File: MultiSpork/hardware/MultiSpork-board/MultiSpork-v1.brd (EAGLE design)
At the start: 160 x 100 mm, 108 parts, among them U1 USD-SOCKETNEW, U2 SAM3SA-MU, U3 MAX11300GTL, U4 MIC2954, U5 MIC5201-3.3BS, U7 MCP73831

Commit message: Updated board with: 	-- Voltage regulators 	-- CC3100 WiFi
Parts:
- added C37, C40, C41, C42, C45, C46, C48, C51, C52, C54, C57, C58, C60, C61, C62: (no value), resistor:C1210
- added C38, C39, C43, C44, C47, C49, C50, C53, C55, C56, C59: (no value), resistor:C0603
- added C63, C67, C69, C70, C71, C73, C74, C75, C76, C77, C80: 100n, resistor:C0603
- added C64, C65, C66: 4u7, resistor:C0603
- added C68, C72: 10u, resistor:C0603
- added C78, C79: 22u, resistor:C1206
- added D15, D16, D17, D18, D19: (no value), diode:SMB
- added JP2: (no value), pinhead:1X06
- added JP3: (no value), pinhead:1X04
- added L10, L12: 2u2, SparkFun-Passives:INDUCTOR-1206
- added L11: 1u, SparkFun-Passives:INDUCTOR-1206
- added L3, L4, L5, L6, L7, L8, L9: NR6028, logos-inductors:NR60XX
- added R1, R14, R15, R16, R17, R18, R19, R20, R21, R22, R23, R24: (no value), resistor:R0603
- added R25, R32: 10K, resistor:R0603
- added R26, R27, R28, R31, R33, R34, R35: 100K, resistor:R0603
- added R29, R30: 4K7, resistor:R0603
- added U6, U8: LT3580EMS8E, MultiSpork-parts:MSOP8
- added U9: CC3100, CC3100:QFN64
- F2: value 500 mA -> 1500 mA
- U4: value MIC2954 -> LT3580EMS8E; device logos-power:SOT223 -> MultiSpork-parts:MSOP8
- U5: value MIC5201-3.3BS -> LT3580EMS8E; device logos-power:SOT223 -> MultiSpork-parts:MSOP8
- moved U3 179.4 mm to (64.8, 30.5)
- moved U5 114.1 mm to (-176.5, -364.5)
- moved U4 58.5 mm to (-168.9, -306.1)
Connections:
- removed net RXD: R6.4
- removed net TXD: R6.6
- new net CC_CS: U2.36, U9.8
- new net CC_INT: R25.2, U2.32, U9.15
- new net CC_NHIB: R28.1, U2.35, U9.2
- new net CC_RST: C80.1, JP2.5, R27.1, U2.24, U9.32
- new net DCDC_ANA2_SW_N: U9.46
- new net DCDC_ANA2_SW_P: U9.45
- new net N$100: JP3.3, U9.59
- new net N$101: JP3.4, U9.58
- new net N$102: R35.2, U9.3
- new net N$106: JP2.1, U9.50
- new net N$107: JP2.2, U9.55
- new net N$108: JP2.3, U9.57
- new net N$109: JP2.4, U9.61
- new net N$18: C38.1, U4.7
- new net N$20: R1.2, U4.6
- new net N$21: R14.1, U4.1
- new net N$22: R15.1, U4.2
- new net N$23: C39.1, R15.2
- new net N$24: C43.1, U5.7
- new net N$25: D16.A, L3.2, U4.4
- new net N$26: R16.2, U5.6
- new net N$28: R17.1, U5.1
- new net N$60: C47.1, R18.1, U5.2
- new net N$61: C44.1, R18.2
- new net N$63: C45.1, L4.2, U5.4
- new net N$64: C45.2, D17.A, L5.1
- new net N$65: C55.1, U8.7
- new net N$66: R22.2, U8.6
- new net N$67: R23.1, U8.1
- new net N$68: C49.1, U6.7
- new net N$69: R19.2, U6.6
- new net N$70: R20.1, U6.1
- new net N$71: C53.1, R21.1, U6.2
- new net N$72: C50.1, R21.2
- new net N$73: C51.1, L6.2, U6.4
- new net N$74: C51.2, D18.A, L7.1
- new net N$75: C59.1, R24.1, U8.2
- new net N$76: C56.1, R24.2
- new net N$77: C58.1, L8.2, U8.4
- new net N$78: C58.2, D19.A, L9.1
- new net N$79: C63.1, U9.54
- new net N$80: C64.1, U9.44
- new net N$81: C66.1, U9.37
- new net N$82: C67.1, C68.1, C69.1, C70.1, C71.1, L10.P$1, U9.10, U9.25, U9.36, U9.48
- new net N$83: C65.1, U9.39
- new net N$84: L10.P$2, U9.38
- new net N$85: C77.1, C78.1, C79.1, U9.33, U9.42
- new net N$87: L11.P$1, U9.40
- new net N$88: L11.P$2, U9.41
- new net N$89: L12.P$2, U9.43
- new net N$90: C72.1, C73.1, C74.1, L12.P$1, U9.56, U9.9
- new net N$91: R31.2, U9.4
- new net N$92: C75.1, U9.49
- new net N$93: C76.1, U9.24
- new net N$94: R32.2, U9.21
- new net N$95: R33.2, U9.34
- new net N$96: R34.2, U9.35
- new net N$98: JP3.1, U9.62
- new net N$99: JP3.2, U9.60
- new net RXD0: R6.4, U2.27
- new net TXD0: R6.6, U2.26
- net +10V: now also C40.1, C41.1, D16.C, R14.2
- net +3V3: now also C52.1, C62.1, D18.C, R20.2, R27.2, R28.2, R29.2, R30.2, U9.47; no longer U5.3
- net +5V: now also C46.1, C61.1, D17.C, R17.2; no longer U4.3
- net +UB: now also D15.A
- net -10V: now also C57.2, C60.2, L9.2, R23.2
- net ACC_CS: now also U2.21
- net GND: now also C37.2, C38.2, C39.2, C40.2, C41.2, C42.2, C43.2, C44.2, C46.2, C47.2, C48.2, C49.2, C50.2, C52.2, C53.2, C54.2, C55.2, C56.2, C57.1, C59.2, C60.1, C61.2, C62.2, C63.2, C64.2, C65.2, C66.2, C67.2, C68.2, C69.2, C70.2, C71.2, C72.2, C73.2, C74.2, C75.2, C76.2, C77.2, C78.2, C79.2, C80.2, D19.C, JP2.6, L5.2, L7.2, R1.1, R16.1, R19.1, R22.1, R25.1, R26.1, R31.1, R32.1, R33.1, R34.1, R35.1, U4.8, U4.EP, U5.8, U5.EP, U6.8, U6.EP, U8.8, U8.EP, U9.PAD
- net MAX_CS: now also U2.20
- net MAX_CVNT: now also U2.23
- net MAX_INT: now also U2.15
- net MISO: now also R26.2, U2.19, U9.7
- net MOSI: now also U2.17, U9.6
- net SCL: now also R30.1, U2.28
- net SCLK: now also U2.16, U9.5
- net SDA: now also R29.1, U2.31
- net SD_CS: now also U2.22
- net V+: now also C37.1, C42.1, C48.1, C54.1, D15.C, L3.1, L4.1, L6.1, L8.1, U4.3, U4.5, U5.3, U5.5, U6.3, U6.5, U8.3, U8.5

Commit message: -- Added flash chip to CC3100.lbr -- Added 2.4 GHz filter to CC3100.lbr -- Added RF components on schematic -- Added CC3100 crystals on schematic -- Added MAX11300 external temperature sensors -- Fixed some issues with the protection circuitry hookup
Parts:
- added C81, C82, C83, C84: (no value), resistor:C0603
- added C85: 100n, resistor:C0603
- added C86, C87: 100u, resistor:CT6032
- added FL1: DEA202450BT, CC3100:DEA202450BT
- added Q2: 40 MHz, logos-crystals:ECX-31B
- added Q3: 32.768 kHz, logos-crystals:CSM-3X
- added Q4, Q5: MMBT3904, SparkFun-DiscreteSemi:SOT23
- added R36: (no value), resistor:R0603
- added R37, R38, R39: 100K, resistor:R0603
- added RESET: SKHMPSE010, switch:SKHMPXE010
- added U$1: ATMEGA128RFA1_MOLEX-ANT, CC3100:ATMEGA128RFA1_MOLEX-ANT
- added U10: M25PX80, CC3100:SOIC8
- moved F10 295.6 mm to (116.8, 34.3)
- moved F11 295.6 mm to (116.8, 30.5)
- moved F12 295.6 mm to (116.8, 26.7)
- moved F3 295.6 mm to (116.8, 61.0)
- moved F4 295.6 mm to (116.8, 57.1)
- moved F5 295.6 mm to (116.8, 53.3)
- moved F6 295.6 mm to (116.8, 49.5)
- moved F7 295.6 mm to (116.8, 45.7)
- moved F8 295.6 mm to (116.8, 41.9)
- moved F9 295.6 mm to (116.8, 38.1)
- moved F22 292.9 mm to (86.4, 26.7)
- moved F20 289.6 mm to (86.4, 29.2)
- moved F21 289.6 mm to (86.4, 25.4)
- moved F18 286.4 mm to (86.4, 31.8)
- moved F19 286.4 mm to (86.4, 27.9)
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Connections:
- new net N$103: C81.1, Q2.1, U9.22
- new net N$104: C82.1, Q2.2, U9.23
- new net N$105: C83.1, Q3.1, U9.52
- new net N$110: C84.1, Q3.2, U9.51
- new net N$111: U10.2, U9.13
- new net N$112: R39.1, U10.1, U9.14
- new net N$113: FL1.1, U9.31
- new net N$114: FL1.3, U$1.A
- new net N$115: Q5.1, Q5.3, U3.19
- new net N$116: Q5.2, U3.20
- new net N$117: Q4.2, U3.13
- new net N$118: Q4.1, Q4.3, U3.12
- new net N$86: R38.2, U10.6, U9.11
- new net N$97: R37.2, U10.5, U9.12
- net +3V3: now also C29.1, C30.1, C85.1, C86.+, C87.+, R36.2, R39.2, U10.3, U10.7, U10.8, U3.2
- net +5V: no longer C29.1, C30.1, U3.2
- net GND: now also C81.2, C82.2, C83.2, C84.2, C85.2, C86.-, C87.-, FL1.2, FL1.4, R37.1, R38.1, RESET.1, RESET.2, RESET.5, U10.4
- net MASTER_RESET: now also R36.1, RESET.3, RESET.4
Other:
- board size 160 x 100 mm -> 100 x 75 mm

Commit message: Finished schematic & placement for the prototype
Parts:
- removed U$1: ATMEGA128RFA1_MOLEX-ANT, CC3100:ATMEGA128RFA1_MOLEX-ANT
- added J1: U.FL, SparkFun-Connectors:U.FL
- added R40: (no value), resistor:R1206
- ANALOG: value (none) -> 76385-316LF; device pinhead-1:2X16SMD/90 -> logos-headers:32P-SIDE-SMD
- C10, C11, C21, C27, C29, C30, C31, C32, C33, C34: device resistor:C1206 -> resistor:C0603
- D16, D18, D19: device diode:SMB -> adafruit:SMADIODE
- D17: device diode:SMB -> adafruit:SOD-123
- L3, L8: value NR6028 -> L-US2323; device logos-inductors:NR60XX -> logos-inductors:L2323
- L4, L5, L6, L7, L9: value NR6028 -> L-US1008; device logos-inductors:NR60XX -> logos-inductors:L1008
- Q2: value 40 MHz -> 32.768 kHz
- Q3: value 32.768 kHz -> 40 MHz
- moved Q5 829.6 mm to (79.5, 27.9)
- moved Q4 827.0 mm to (75.9, 27.9)
- moved C87 817.1 mm to (42.4, 32.0), turned to 180 degrees
- moved C86 814.7 mm to (42.4, 35.8), turned to 180 degrees
- moved RESET 812.7 mm to (68.6, 66.3), turned to 270 degrees
- moved R36 808.3 mm to (63.0, 68.6), turned to 180 degrees
- moved FL1 786.9 mm to (49.0, 10.4), turned to 180 degrees
- moved C85 772.4 mm to (17.0, 16.5), turned to 90 degrees
- moved R39 771.9 mm to (23.1, 7.87), turned to 180 degrees
- moved R38 768.0 mm to (18.8, 16.5), turned to 270 degrees
- moved R37 762.4 mm to (20.6, 16.5), turned to 270 degrees
- moved C84 761.2 mm to (49.8, 27.2), turned to 90 degrees
- moved C83 756.8 mm to (47.2, 27.2), turned to 90 degrees
- moved U10 750.6 mm to (23.4, 11.7), turned to 90 degrees
- moved JP3 736.3 mm to (39.9, 40.9)
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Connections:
- removed net N$56 (its old number): F7.2, F8.2, F9.2
- removed net N$59: F10.2, F11.2, F12.2, F13.2
- removed net N$62: F14.2, F15.2, F16.2
- removed net PORT0: F3.2
- removed net PORT1: F4.2
- removed net PORT2: F5.2
- removed net PORT3: F6.2
- net ACC_CS: now also R6.4; no longer R7.7
- net AGND: now also R40.1
- net GND: now also J1.P$1, J1.P$2, R40.2
- net MISO: now also R2.2, R6.8; no longer R2.8, R7.5
- net MOSI: now also R2.6; no longer R2.4
- net N$10: now also R7.6; no longer R7.4
- net N$103: now also Q3.1; no longer Q2.1
- net N$104: now also Q3.2; no longer Q2.2
- net N$105: now also Q2.1; no longer Q3.1
- net N$11: now also R6.7; no longer R7.6
- net N$110: now also Q2.2; no longer Q3.2
- net N$114: now also J1.P$3; no longer U$1.A
- net N$12: now also R6.3; no longer R7.8
- net N$13: now also R6.1; no longer R6.2
- net N$14: now also R7.8; no longer R6.5
- net N$15: now also R7.4; no longer R6.3
- net N$16: now also R6.5; no longer R6.7
- net N$2: now also R2.7; no longer R2.1
- net N$25: now also L3.4; no longer L3.2
- net N$4: now also R2.5; no longer R2.3
- net N$5: now also R2.3; no longer R2.5
- net N$6: now also R2.1; no longer R2.7
- net N$77: now also L8.4; no longer L8.2
- net PORT00: now also F3.2
- net PORT01: now also F4.2
- net PORT02: now also F5.2
- net PORT03: now also F6.2
- net PORT04: now also F7.2
- net PORT05: now also F8.2
- net PORT06: now also F9.2
- net PORT07: now also F10.2
- net PORT08: now also F11.2
- net PORT09: now also F12.2
- net PORT10: now also F13.2
- net PORT11: now also F14.2
- net PORT12: now also F15.2
- net PORT13: now also F16.2
- net RXD0: now also R7.3; no longer R6.4
- net SCL: now also R6.6; no longer R6.8
- net SCLK: now also R2.4, R7.5; no longer R2.6, R7.3
- net SDA: now also R6.2; no longer R6.1
- net SD_CS: now also R2.8; no longer R2.2
- net TXD0: now also R7.7; no longer R6.6
- net V+: now also L3.3, L8.3; no longer L3.1, L8.1
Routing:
- added copper zone on layer 1, net AGND
- added copper zone on layer 16, net AGND
- added copper zone on layer 1, net GND
- added copper zone on layer 16, net GND
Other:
- board size 100 x 75 mm -> 101.6 x 76.2 mm

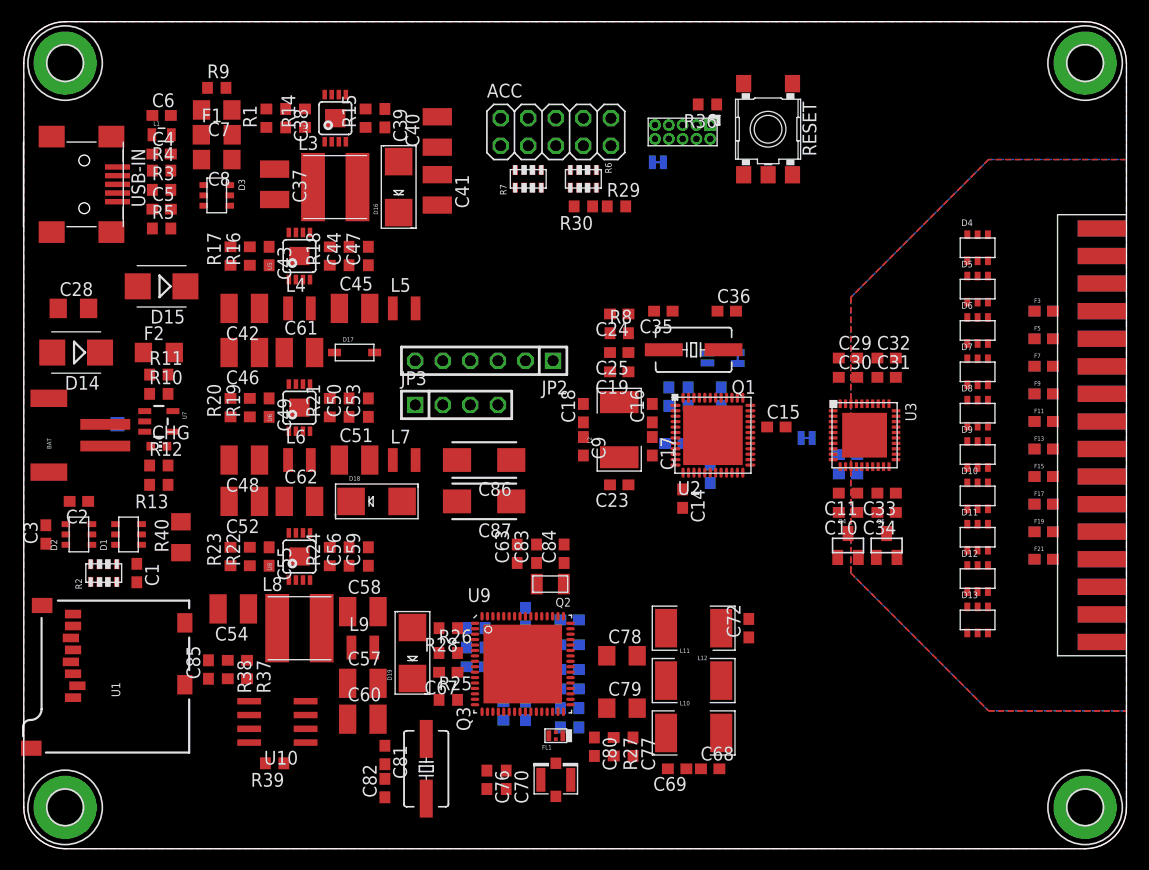
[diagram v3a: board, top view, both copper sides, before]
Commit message: Shrank the board from 3x4 to 3x3.4
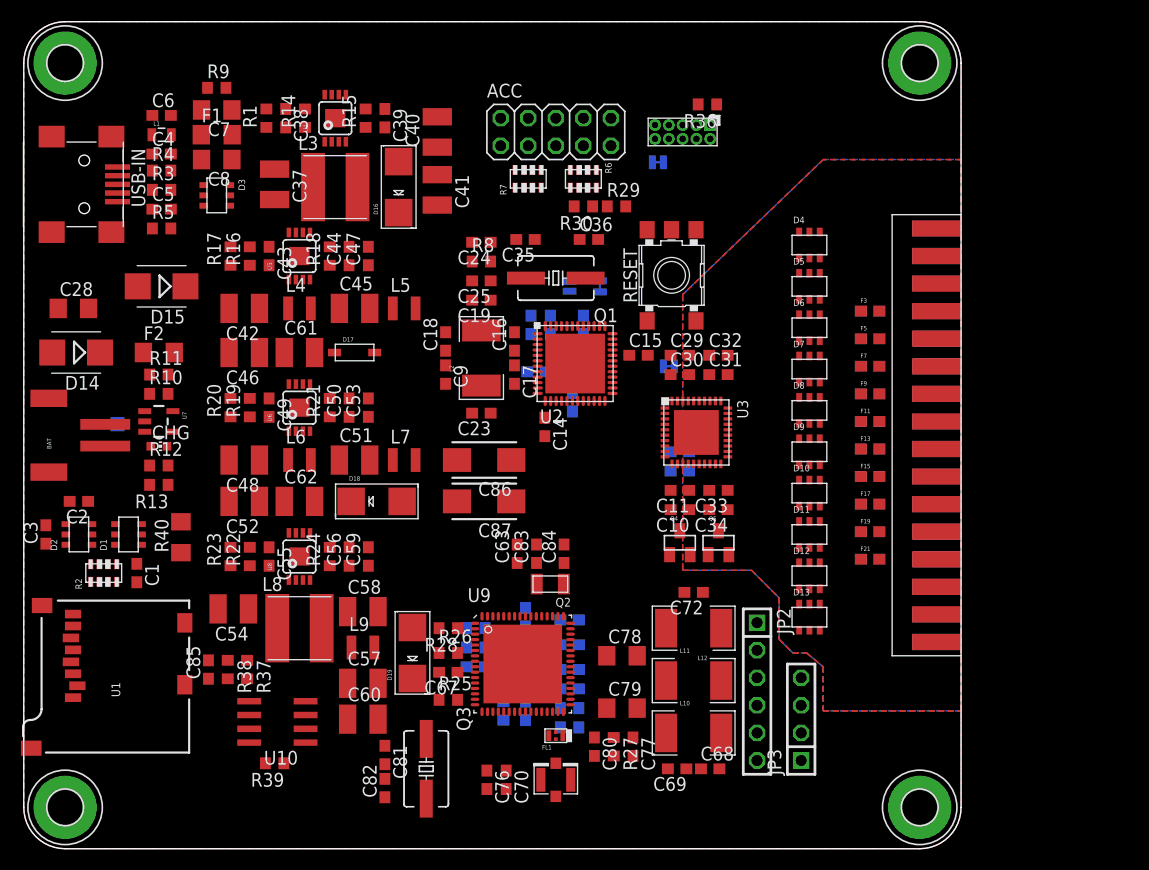
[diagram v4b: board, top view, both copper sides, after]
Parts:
- moved JP3 43.0 mm to (71.6, 11.9), turned to 90 degrees
- moved JP2 39.5 mm to (67.6, 14.5), turned to 270 degrees
- moved RESET 16.1 mm to (59.7, 52.8), turned to 90 degrees
- moved F10 16.0 mm to (78.0, 41.9)
- moved F11 16.0 mm to (78.0, 39.4)
- moved F12 16.0 mm to (78.0, 39.4)
- moved F13 16.0 mm to (78.0, 36.8)
- moved F14 16.0 mm to (78.0, 36.8)
- moved F15 16.0 mm to (78.0, 34.3)
- moved F16 16.0 mm to (78.0, 34.3)
- moved F17 16.0 mm to (78.0, 31.8)
- moved F18 16.0 mm to (78.0, 31.8)
- moved F19 16.0 mm to (78.0, 29.2)
- moved F20 16.0 mm to (78.0, 29.2)
- moved F21 16.0 mm to (78.0, 26.7)
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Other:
- board size 101.6 x 76.2 mm -> 86.4 x 76.2 mm

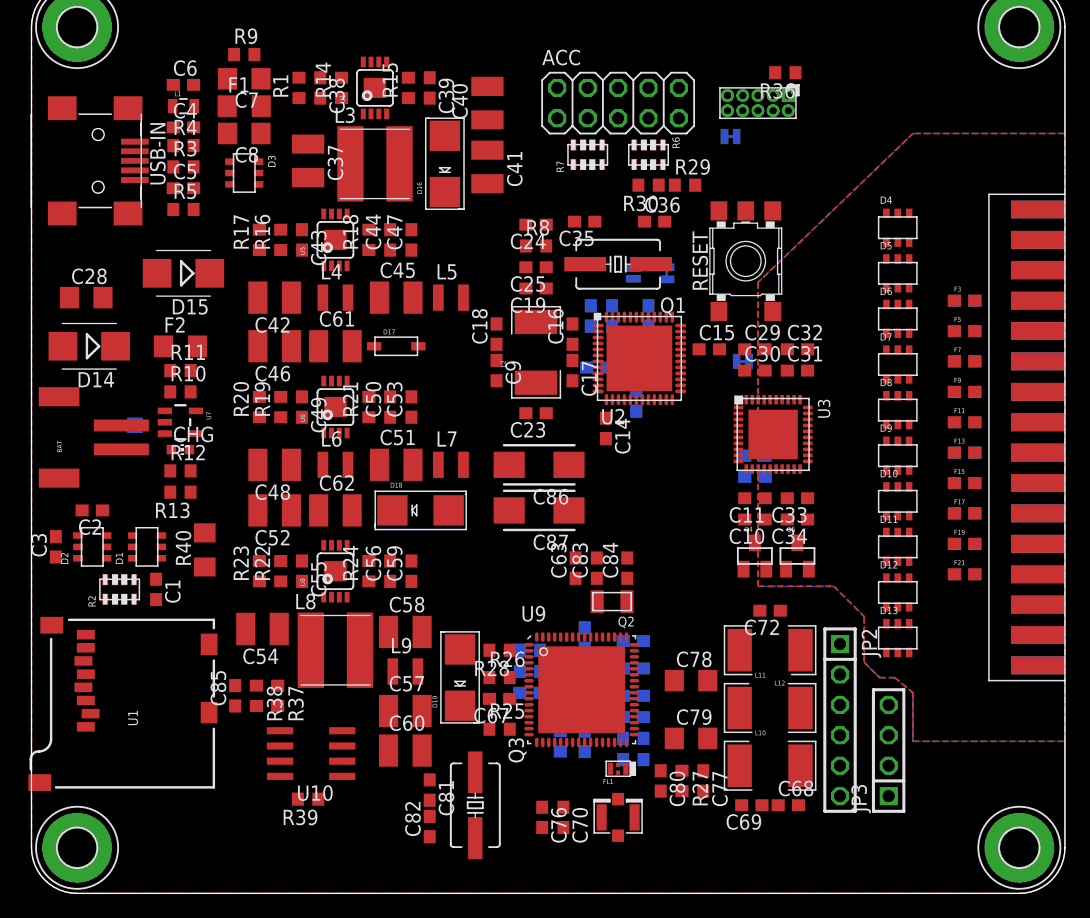
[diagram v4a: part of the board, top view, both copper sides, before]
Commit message: -- Updated MAX11300 footprint with rounded pads to account for minimum clearances at the corners -- Added a switch to turn the regulators on and off -- Routed USB -- Routed SPI busses -- Routed analog inputs to protection components
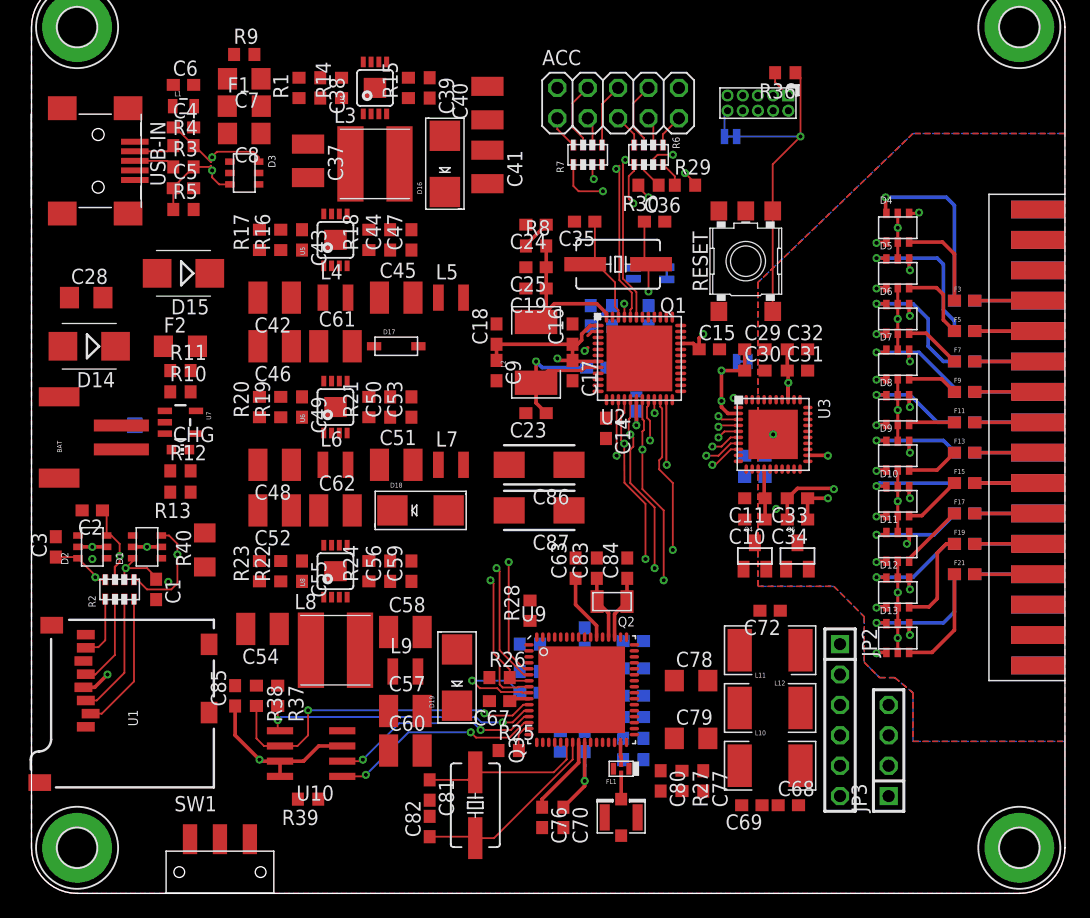
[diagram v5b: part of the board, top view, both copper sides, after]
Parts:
- added SW1: JS102011SAQN, logos-switch:JS102011SAQN
- moved R28 4.17 mm to (41.7, 23.6), turned to 90 degrees
- moved R25 1.93 mm to (39.9, 11.9)
- moved R35 0.51 mm to (41.7, 20.8)
- moved FL1 0.25 mm to (49.3, 10.4)
- moved J1 0.25 mm to (49.3, 6.35)
- moved D19 0.25 mm to (35.6, 18.0)
- moved C67 0.19 mm to (39.1, 16.1)
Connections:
- new net SHTDWN: SW1.2, U4.5, U5.5, U6.5, U8.5
- net GND: now also SW1.1
- net V+: now also SW1.3; no longer U4.5, U5.5, U6.5, U8.5
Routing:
- net MISO: track 0.00 -> 113.0 mm, vias 0 -> 6
- net MOSI: track 0.00 -> 110.7 mm, vias 0 -> 6
- net SCLK: track 0.00 -> 110.4 mm, vias 0 -> 6
- net SD_CS: track 0.00 -> 64.1 mm, vias 0 -> 2
- net USB_N: track 0.00 -> 58.2 mm, vias 0 -> 2
- net +3V3: track 0.00 -> 57.1 mm, vias 0 -> 10
- net USB_P: track 0.00 -> 56.9 mm, vias 0 -> 2
- net +10V: track 0.00 -> 40.9 mm, vias 0 -> 9
- net -10V: track 0.00 -> 34.2 mm, vias 0 -> 22
- net N$86: track 0.00 -> 28.8 mm, vias 0 -> 2
- net MASTER_RESET: track 0.00 -> 26.4 mm, vias 0 -> 1
- net ACC_CS: track 0.00 -> 25.6 mm, vias 0 -> 2
- net N$97: track 0.00 -> 23.8 mm, vias 0 -> 2
- net VDDCORE: track 0.00 -> 18.1 mm, vias 0 -> 2
- net N$112: track 0.00 -> 17.8 mm, vias 0 -> 2
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- added copper zone on layer 2, net +10V
- added copper zone on layer 15, net +3V3
- added copper zone on layer 15, net -10V
- added copper zone on layer 2, net GND
